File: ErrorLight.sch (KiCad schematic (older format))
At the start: 15 parts, among them J11 ErrorLightConn, Q3 NTR4003NT1G, Q4 VND5N07-E, U12 SI8261ABC-IS

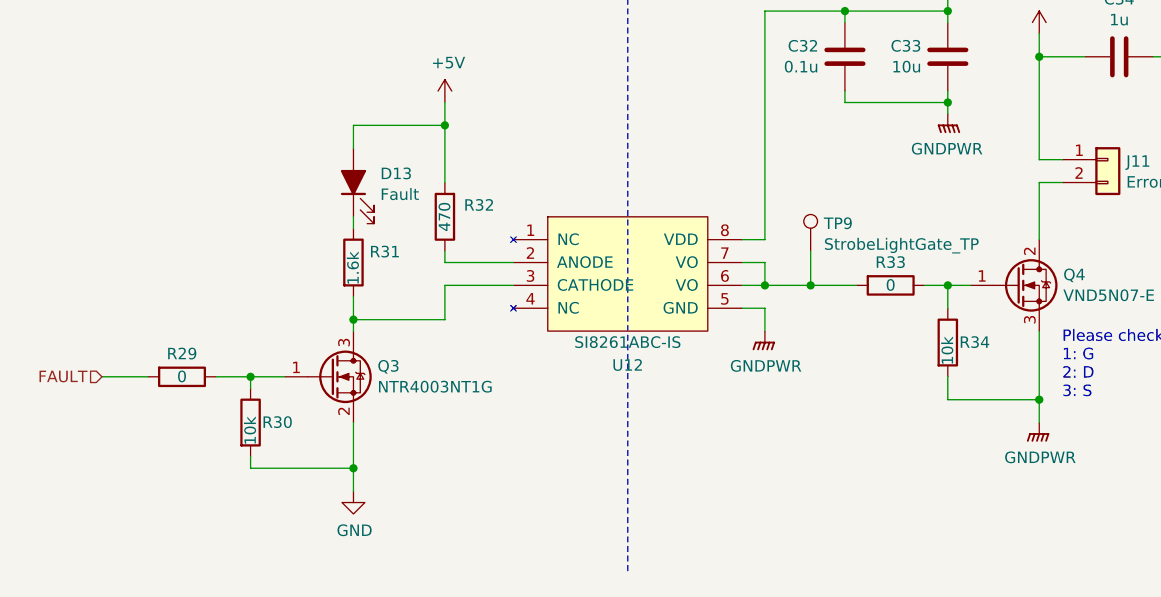
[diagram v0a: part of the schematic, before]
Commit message: Updates BAS70-04 footprint for Contactor auxillary interface
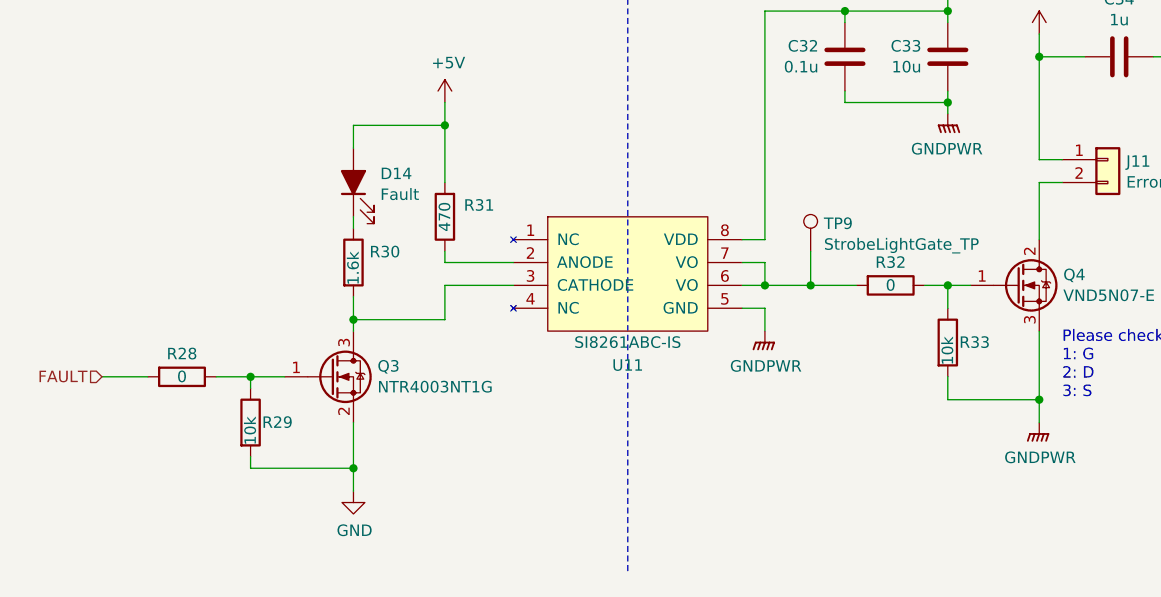
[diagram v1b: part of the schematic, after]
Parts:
- renumbered D13 to D14, R29 to R28, R30 to R29, R31 to R30, R32 to R31, R33 to R32, R34 to R33, U12 to U11
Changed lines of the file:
@@
 P 4450 3650
 AR Path="/5C392C6A/5D93094B" Ref="R?"  Part="1"
-AR Path="/5D923D59/5D93094B" Ref="R32"  Part="1"
-F 0 "R32" H 4300 3600 50  0000 C CNN
+AR Path="/5D923D59/5D93094B" Ref="R31"  Part="1"
+F 0 "R31" H 4300 3600 50  0000 C CNN
 F 1 "470" V 4450 3650 50  0000 C CNN
 F 2 "Resistor_SMD:R_0805_2012Metric" V 4380 3650 50  0001 C CNN
@@
 P 6650 2700
 AR Path="/5C392C6A/5D930954" Ref="#PWR?"  Part="1"
-AR Path="/5D923D59/5D930954" Ref="#PWR068"  Part="1"
-F 0 "#PWR068" H 6650 2550 50  0001 C CNN
+AR Path="/5D923D59/5D930954" Ref="#PWR070"  Part="1"
+F 0 "#PWR070" H 6650 2550 50  0001 C CNN
 F 1 "+12V" H 6665 2873 50  0000 C CNN
 F 2 "" H 6650 2700 50  0001 C CNN
@@
 P 6650 3200
 AR Path="/5C392C6A/5D930960" Ref="#PWR?"  Part="1"
-AR Path="/5D923D59/5D930960" Ref="#PWR069"  Part="1"
-F 0 "#PWR069" H 6650 3000 50  0001 C CNN
+AR Path="/5D923D59/5D930960" Ref="#PWR071"  Part="1"
+F 0 "#PWR071" H 6650 3000 50  0001 C CNN
 F 1 "GNDPWR" H 6654 3046 50  0000 C CNN
 F 2 "" H 6650 3150 50  0001 C CNN
@@
 P 5850 4150
 AR Path="/5C392C6A/5D93097A" Ref="#PWR?"  Part="1"
-AR Path="/5D923D59/5D93097A" Ref="#PWR067"  Part="1"
-F 0 "#PWR067" H 5850 3950 50  0001 C CNN
+AR Path="/5D923D59/5D93097A" Ref="#PWR069"  Part="1"
+F 0 "#PWR069" H 5850 3950 50  0001 C CNN
 F 1 "GNDPWR" H 5854 3996 50  0000 C CNN
 F 2 "" H 5850 4100 50  0001 C CNN
@@
 AR Path="/5C38C674/5D930982" Ref="#PWR?"  Part="1"
 AR Path="/5C392C6A/5D930982" Ref="#PWR?"  Part="1"
-AR Path="/5D923D59/5D930982" Ref="#PWR070"  Part="1"
-F 0 "#PWR070" H 7050 2700 50  0001 C CNN
+AR Path="/5D923D59/5D930982" Ref="#PWR072"  Part="1"
+F 0 "#PWR072" H 7050 2700 50  0001 C CNN
 F 1 "+12V" H 7065 3023 50  0000 C CNN
 F 2 "" H 7050 2850 50  0001 C CNN
@@
 AR Path="/5C38C674/5D930988" Ref="R?"  Part="1"
 AR Path="/5C392C6A/5D930988" Ref="R?"  Part="1"
-AR Path="/5D923D59/5D930988" Ref="R34"  Part="1"
-F 0 "R34" H 6700 4200 50  0000 L CNN
+AR Path="/5D923D59/5D930988" Ref="R33"  Part="1"
+F 0 "R33" H 6700 4200 50  0000 L CNN
 F 1 "10k" V 6650 4100 50  0000 L CNN
 F 2 "Resistor_SMD:R_0805_2012Metric" V 6580 4200 50  0001 C CNN
@@
 AR Path="/5C38C674/5D930995" Ref="R?"  Part="1"
 AR Path="/5C392C6A/5D930995" Ref="R?"  Part="1"
-AR Path="/5D923D59/5D930995" Ref="R33"  Part="1"
-F 0 "R33" V 6300 3950 50  0000 C CNN
+AR Path="/5D923D59/5D930995" Ref="R32"  Part="1"
+F 0 "R32" V 6300 3950 50  0000 C CNN
 F 1 "0" V 6400 3950 50  0000 C CNN
 F 2 "Resistor_SMD:R_0805_2012Metric" V 6330 3950 50  0001 C CNN
@@
 AR Path="/5C38C674/5D9309B4" Ref="R?"  Part="1"
 AR Path="/5C392C6A/5D9309B4" Ref="R?"  Part="1"
-AR Path="/5D923D59/5D9309B4" Ref="R31"  Part="1"
-F 0 "R31" H 4120 3896 50  0000 L CNN
+AR Path="/5D923D59/5D9309B4" Ref="R30"  Part="1"
+F 0 "R30" H 4120 3896 50  0000 L CNN
 F 1 "1.6k" V 4050 3750 50  0000 L CNN
 F 2 "Resistor_SMD:R_0805_2012Metric" V 3980 3850 50  0001 C CNN
@@
 AR Path="/5C38C674/5D9309BC" Ref="#PWR?"  Part="1"
 AR Path="/5C392C6A/5D9309BC" Ref="#PWR?"  Part="1"
-AR Path="/5D923D59/5D9309BC" Ref="#PWR071"  Part="1"
-F 0 "#PWR071" H 7050 4350 50  0001 C CNN
+AR Path="/5D923D59/5D9309BC" Ref="#PWR073"  Part="1"
+F 0 "#PWR073" H 7050 4350 50  0001 C CNN
 F 1 "GNDPWR" H 7054 4396 50  0000 C CNN
 F 2 "" H 7050 4500 50  0001 C CNN
@@
 AR Path="/5C38C674/5D9309C8" Ref="#PWR?"  Part="1"
 AR Path="/5C392C6A/5D9309C8" Ref="#PWR?"  Part="1"
-AR Path="/5D923D59/5D9309C8" Ref="#PWR072"  Part="1"
-F 0 "#PWR072" H 7750 2800 50  0001 C CNN
+AR Path="/5D923D59/5D9309C8" Ref="#PWR074"  Part="1"
+F 0 "#PWR074" H 7750 2800 50  0001 C CNN
 F 1 "GNDPWR" H 7754 2846 50  0000 C CNN
 F 2 "" H 7750 2950 50  0001 C CNN
@@
 AR Path="/5D9309DA" Ref="D?"  Part="1"
 AR Path="/5C392C6A/5D9309DA" Ref="D?"  Part="1"
-AR Path="/5D923D59/5D9309DA" Ref="D13"  Part="1"
-F 0 "D13" V 4088 3383 50  0000 R CNN
+AR Path="/5D923D59/5D9309DA" Ref="D14"  Part="1"
+F 0 "D14" V 4088 3383 50  0000 R CNN
 F 1 "Fault" V 3997 3383 50  0000 R CNN
 F 2 "LED_SMD:LED_0805_2012Metric" H 4050 3500 50  0001 C CNN
@@
 P 4050 4850
 AR Path="/5C392C6A/5D9309F1" Ref="#PWR?"  Part="1"
-AR Path="/5D923D59/5D9309F1" Ref="#PWR065"  Part="1"
-F 0 "#PWR065" H 4050 4600 50  0001 C CNN
+AR Path="/5D923D59/5D9309F1" Ref="#PWR067"  Part="1"
+F 0 "#PWR067" H 4050 4600 50  0001 C CNN
 F 1 "GND" H 4055 4677 50  0000 C CNN
 F 2 "" H 4050 4850 50  0001 C CNN
@@
 P 4450 3150
 AR Path="/5C392C6A/5D930A01" Ref="#PWR?"  Part="1"
-AR Path="/5D923D59/5D930A01" Ref="#PWR066"  Part="1"
-F 0 "#PWR066" H 4450 3000 50  0001 C CNN
+AR Path="/5D923D59/5D930A01" Ref="#PWR068"  Part="1"
+F 0 "#PWR068" H 4450 3000 50  0001 C CNN
 F 1 "+5V" H 4465 3323 50  0000 C CNN
 F 2 "" H 4450 3150 50  0001 C CNN
@@
 AR Path="/5C38C674/5D930A07" Ref="R?"  Part="1"
 AR Path="/5C392C6A/5D930A07" Ref="R?"  Part="1"
-AR Path="/5D923D59/5D930A07" Ref="R29"  Part="1"
-F 0 "R29" V 3200 4350 50  0000 C CNN
+AR Path="/5D923D59/5D930A07" Ref="R28"  Part="1"
+F 0 "R28" V 3200 4350 50  0000 C CNN
 F 1 "0" V 3300 4350 50  0000 C CNN
 F 2 "Resistor_SMD:R_0805_2012Metric" V 3230 4350 50  0001 C CNN
@@
 AR Path="/5C38C674/5D930A0D" Ref="R?"  Part="1"
 AR Path="/5C392C6A/5D930A0D" Ref="R?"  Part="1"
-AR Path="/5D923D59/5D930A0D" Ref="R30"  Part="1"
-F 0 "R30" H 3650 4550 50  0000 L CNN
+AR Path="/5D923D59/5D930A0D" Ref="R29"  Part="1"
+F 0 "R29" H 3650 4550 50  0000 L CNN
 F 1 "10k" V 3600 4450 50  0000 L CNN
 F 2 "Resistor_SMD:R_0805_2012Metric" V 3530 4550 50  0001 C CNN
@@
 	5850 2750 6200 2750
 $Comp
-L utsvt-bps:SI8261ABC-IS U12
+L utsvt-bps:SI8261ABC-IS U11
 U 1 1 5F13FC4D
 P 5250 3650
-F 0 "U12" H 5250 3000 50  0000 C CNN
+F 0 "U11" H 5250 3000 50  0000 C CNN
 F 1 "SI8261ABC-IS" H 5250 3100 50  0000 C CNN
 F 2 "Package_SO:SOIC-8_3.9x4.9mm_P1.27mm" H 5250 3650 50  0001 C CNN
